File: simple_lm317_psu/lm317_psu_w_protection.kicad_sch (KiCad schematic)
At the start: 10 parts, among them J1 Bornera, U1 LM317

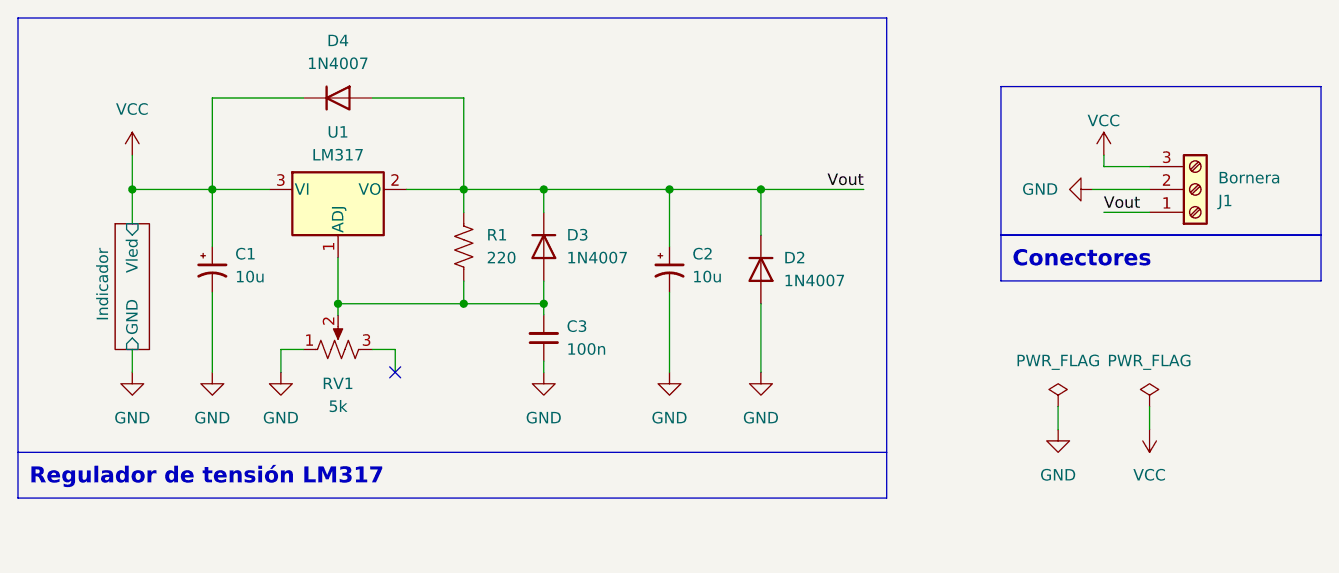
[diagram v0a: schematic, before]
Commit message: Simple PSU LM317 based
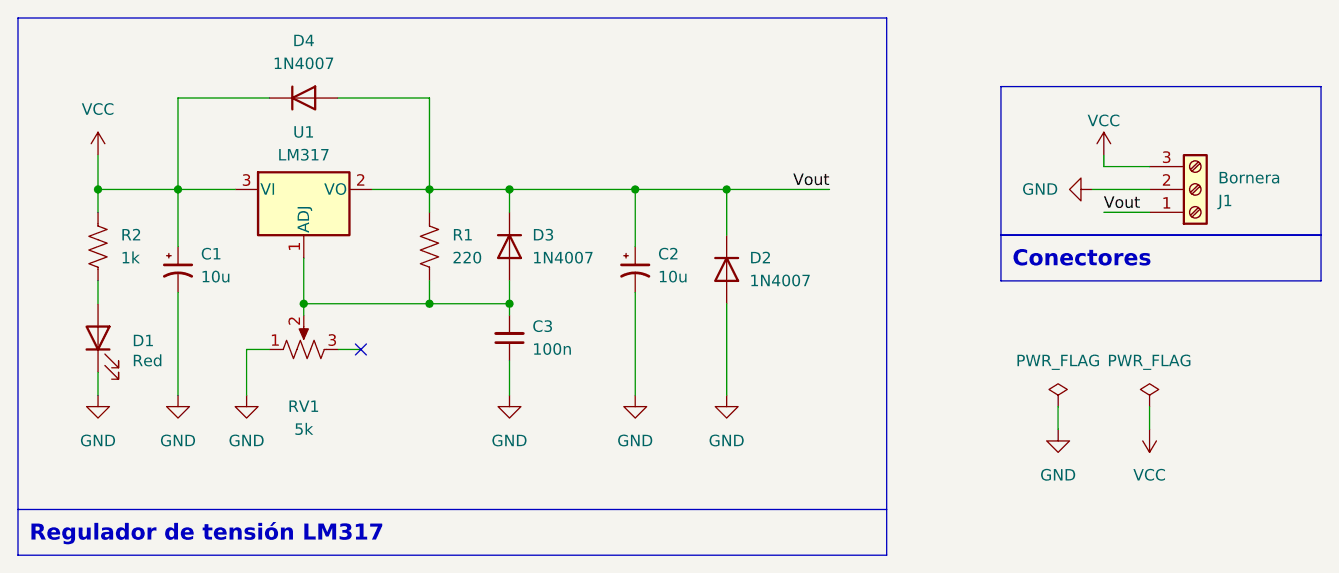
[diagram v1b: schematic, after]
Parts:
- added D1: Red, LED_THT:LED_D5.0mm, symbol Device:LED
- added R2: 1k, Resistor_THT:R_Axial_DIN0207_L6.3mm_D2.5mm_P7.62mm_Horizontal, symbol Device:R_US
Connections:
- net GND: now also D1.1 (K)
- net VCC: now also R2.1
- new net: D1.2 (A), R2.2
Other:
- removed sheet Indicador
- moved on the sheet: C1, C2, C3, D2, D3, D4, R1, RV1, U1
